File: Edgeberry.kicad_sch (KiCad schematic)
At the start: 28 parts, among them J1 Molex_KK_1x02_P2.54mm, J2 Raspberry_Pi_2_3, J3 Edgeberry Cartridge Connector, P1 12Vin, Q1 BC547, Q2 BC547, Q3 BC547, SW1 SW_PUSH, U1 24LC256, U2 LM2596S-5.0

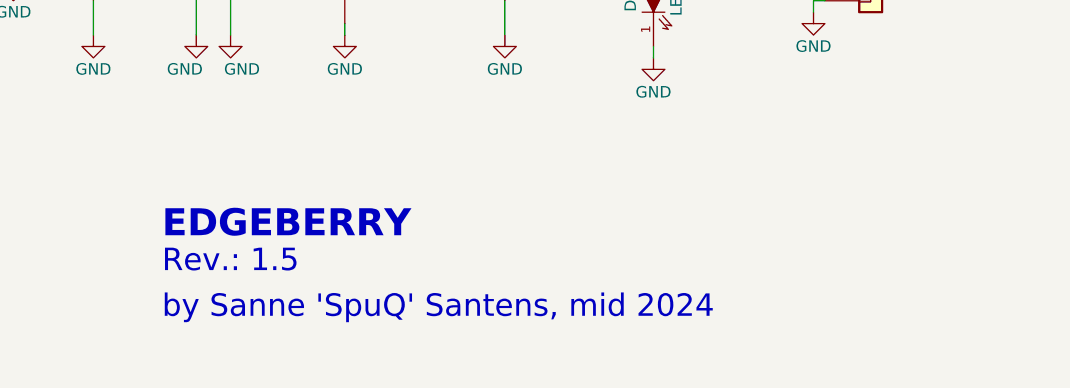
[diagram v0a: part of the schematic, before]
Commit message: Open Source Hardware license: CERN-OHL-W
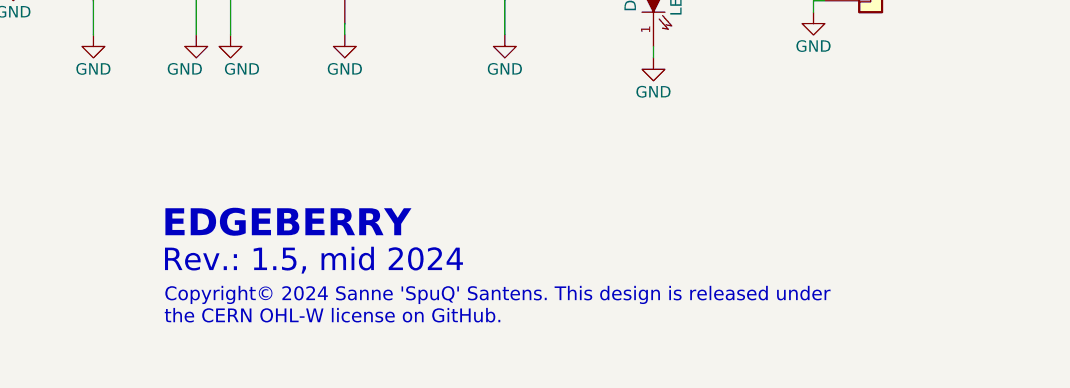
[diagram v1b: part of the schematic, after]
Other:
- note added: "Copyright© 2024 Sanne 'SpuQ' Santens. This design is released under the CERN OHL-W license on GitHub."
- note added: "Rev.: 1.5, mid 2024"
- note removed: "Rev.: 1.5"
- note removed: "by Sanne 'SpuQ' Santens, mid 2024"
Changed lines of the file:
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@@
+		)
+	)
+	(text "Copyright© 2024 Sanne 'SpuQ' Santens. This design is released under\nthe CERN OHL-W license on GitHub."
+		(exclude_from_sim no)
+		(at 181.864 178.816 0)
+		(effects
+			(font
+				(size 1.524 1.524)
+			)
+			(justify left)
 		)
 	)
@@
 			(font
 				(size 1.524 1.524)
-			)
-			(justify left bottom)
-		)
-	)
-	(text "by Sanne 'SpuQ' Santens, mid 2024"
-		(exclude_from_sim no)
-		(at 181.61 180.34 0)
-		(effects
-			(font
-				(size 2.4892 2.4892)
 			)
 			(justify left bottom)
@@
 		)
 	)
-	(text "Rev.: 1.5"
+	(text "Rev.: 1.5, mid 2024\n"
 		(exclude_from_sim no)
 		(at 181.61 175.26 0)

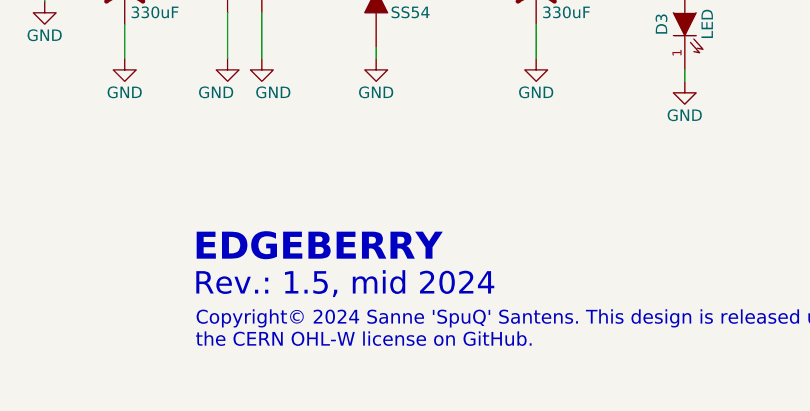
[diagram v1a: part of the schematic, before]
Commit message: Buck convertor: Schottky diode footprint modification
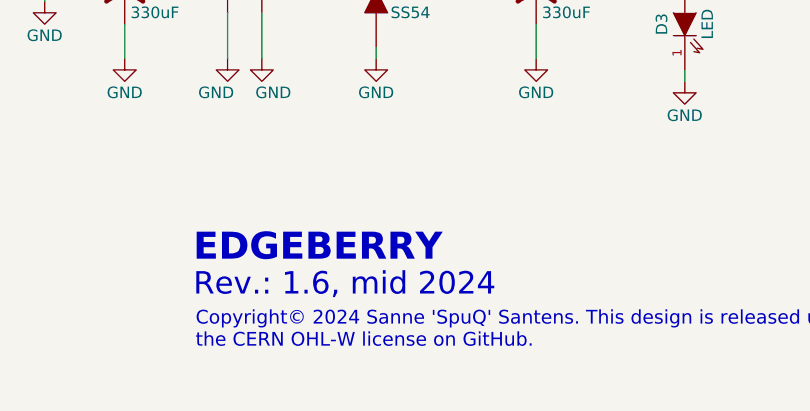
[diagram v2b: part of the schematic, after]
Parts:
- D2: footprint emcosys:SS54_Schottky_40V_5A -> Diode_SMD:D_SMA
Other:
- note added: "Rev.: 1.6, mid 2024"
- note removed: "Rev.: 1.5, mid 2024"
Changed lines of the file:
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@@
 		)
 	)
-	(text "Rev.: 1.5, mid 2024\n"
+	(text "Rev.: 1.6, mid 2024\n"
 		(exclude_from_sim no)
 		(at 181.61 175.26 0)
@@
 			)
 		)
-		(property "Footprint" "emcosys:SS54_Schottky_40V_5A"
+		(property "Footprint" "Diode_SMD:D_SMA"
 			(at 201.93 142.24 0)
 			(effects

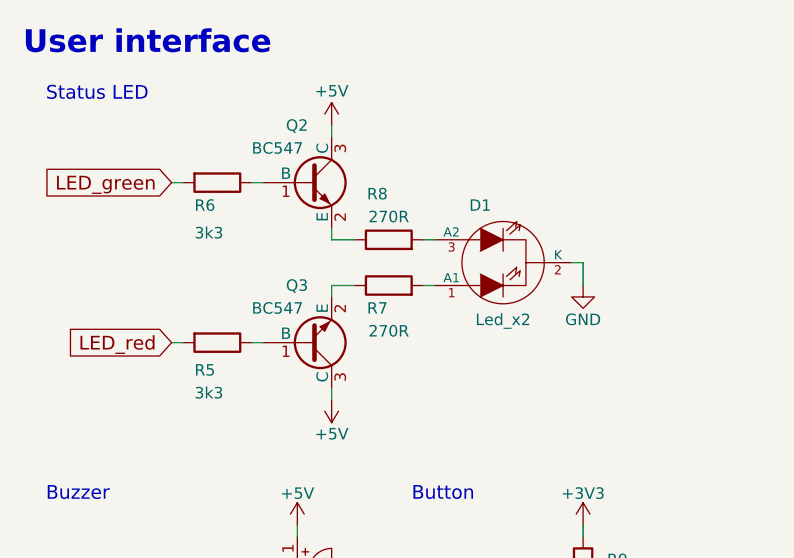
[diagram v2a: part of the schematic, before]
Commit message: Bugfix: R7 and R8 lower resistors as temp fix
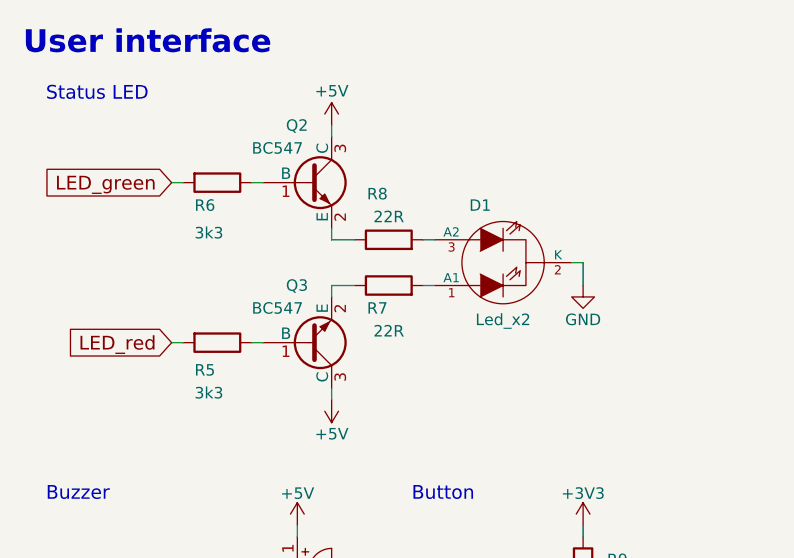
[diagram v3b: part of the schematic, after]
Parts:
- R7, R8: value 270R -> 22R
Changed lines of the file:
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@@
 			)
 		)
-		(property "Value" "270R"
+		(property "Value" "22R"
 			(at 60.96 39.37 90)
 			(effects
@@
 			)
 		)
-		(property "Value" "270R"
+		(property "Value" "22R"
 			(at 60.96 52.07 90)
 			(effects

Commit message: Edgeberry rev1.7
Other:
- note added: "12V - 24V Power to 5V"
- note added: "Base Board Rev. 1.7, late 2024"
- note added: "Compatible with the 40-pin Raspberry PI GPIO header. Tested with RPi models 3B, 3B+, 4B, 5B"
- note added: "RPi HAT ID EEPROM"
- note removed: "12V Power to 5V"
- note removed: "Compatible with the 40-pin Raspberry PI GPIO header. Tested with RPi models 3B, 3B+, 4B"
- note removed: "RPi Hat ID EEPROM"
- note removed: "Rev.: 1.6, mid 2024"
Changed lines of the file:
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@@
+		)
+	)
+	(text "Base Board Rev. 1.7, late 2024"
+		(exclude_from_sim no)
+		(at 181.864 175.006 0)
+		(effects
+			(font
+				(face "Lato Black")
+				(size 2.159 2.159)
+			)
+			(justify left)
 		)
 	)
@@
 		)
 	)
-	(text "12V Power to 5V"
+	(text "12V - 24V Power to 5V"
 		(exclude_from_sim no)
 		(at 144.78 116.84 0)
@@
 		)
 	)
-	(text "RPi Hat ID EEPROM"
+	(text "RPi HAT ID EEPROM"
 		(exclude_from_sim no)
 		(at 20.32 116.84 0)
@@
 		)
 	)
-	(text "Rev.: 1.6, mid 2024\n"
-		(exclude_from_sim no)
-		(at 181.61 175.26 0)
-		(effects
-			(font
-				(size 2.4892 2.4892)
-			)
-			(justify left bottom)
-		)
-	)
 	(text "Only for programming the EEPROM with the 'hat'\ninformation the WP pin (Write Protection) must\nbe pulled low by the manufacturer. For normal\nuse, write protection is enabled by pulling the\npull-up resistor"
 		(exclude_from_sim no)
@@
 	(text "EDGEBERRY"
 		(exclude_from_sim no)
-		(at 181.61 171.45 0)
+		(at 181.61 173.736 0)
 		(effects
 			(font
-				(size 3 3)
+				(face "Lato Heavy")
+				(size 4.572 4.572)
 				(thickness 0.4)
 				(bold yes)
@@
 		)
 	)
-	(text "Compatible with the 40-pin Raspberry PI GPIO header.\nTested with RPi models 3B, 3B+, 4B"
+	(text "Compatible with the 40-pin Raspberry PI GPIO header.\nTested with RPi models 3B, 3B+, 4B, 5B"
 		(exclude_from_sim no)
 		(at 116.84 26.67 0)
